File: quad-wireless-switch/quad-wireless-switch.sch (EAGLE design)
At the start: 69 parts, among them IC1 LM2937IMP-3.3, Q1 DN2625K4-G, Q2 SI2323DS-T1-E3, Q3 IRL520, Q4 IRL520, Q5 IRL520, Q6 IRL520, U1 ATMEGA328P_TQFP

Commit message: quad wireless switch wip
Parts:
- added D3, D4, D5, D6: 1N4004, diode:1N4004
- added OK1, OK2, OK3, OK4: 4N35SM, optocoupler:4N35SM
- added R24, R28, R29: 220, microbuilder:RESISTOR0805
- added R25, R26, R30, R31: 10K, microbuilder:RESISTOR0805
- added R27: 150, microbuilder:RESISTOR0805
- R10, R16: value 10k -> 10K
- R11: value 10k -> 150
- R13, R20, R21, R22: value 150 -> 220
- R14: value 10k -> 220
- R15, R23: value 150 -> 10K
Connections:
- removed net OUT2_GATE: Q4.G, R13.2
- removed net OUT3_GATE: Q5.G, R15.2
- removed net OUT4_GATE: Q6.G, R17.2
- new net N$21: OK1.COL, R25.1
- new net N$23: OK1.A, R24.1
- new net N$24: D5.A, OUT3-1.KL, Q5.D
- new net N$25: LED3.C, R21.1
- new net N$26: OK3.COL, R23.1
- new net N$27: OK3.A, R22.1
- new net N$28: OK3.EMI, R17.1, R26.2
- new net N$29: D6.A, OUT4-1.KL, Q6.D
- new net N$30: LED4.C, R28.1
- new net N$31: OK4.COL, R30.1
- new net N$32: OK4.A, R29.1
- new net N$33: OK4.EMI, R27.1, R31.2
- net 12V: now also D3.C, D4.C, D5.C, D6.C, R15.2, R23.2, R25.2, R30.2
- net GND: now also OK1.C, OK2.C, OK3.C, OK4.C, R10.1, R13.2, R16.1, R26.1, R28.2, R31.1; no longer R10.2, R11.2, R14.2, R16.2, R22.2, R23.2
- net N$18: now also OK2.A, R14.1; no longer OUT3-1.KL, Q5.D
- net N$2: now also OK1.EMI, R10.2, R12.1; no longer LED2.C, R21.1
- net N$22: now also OK2.EMI, R11.1, R16.2; no longer OUT4-1.KL, Q6.D
- net N$3: now also D4.A, OUT2-1.KL, Q4.D; no longer LED3.C, R22.1
- net N$4: now also LED2.C, R13.1; no longer LED4.C, R23.1
- net N$6: now also D3.A
- net N$8: now also OK2.COL, R15.1; no longer OUT2-1.KL, Q4.D
- net OUT1: now also R24.2; no longer R10.1, R12.1
- net OUT1_GATE: now also Q4.G, Q5.G, Q6.G, R11.2, R17.2, R27.2
- net OUT2: now also R14.2; no longer R11.1, R13.1
- net OUT3: now also R22.2; no longer R14.1, R15.1
- net OUT4: now also R29.2; no longer R16.1, R17.1
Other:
- moved on the sheet: LED1, LED2, LED3, LED4, OUT1-1, OUT1-2, OUT2-1, OUT2-2, OUT3-1, OUT3-2, OUT4-1, OUT4-2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

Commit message: wip
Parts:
- R1: value 10k -> 100k
- R10, R23, R25: value 10K -> 220
- R11, R12: value 150 -> 10k
- R14, R28, R29: value 220 -> 10K
- R17, R27: value 150 -> 10K
- R18, R19: value 10k -> 150
- R2: value 10k -> 39k
- R20, R21: value 220 -> 10k
- R3: value 100k -> 10k
- R30, R31: value 10K -> 150
- R4: value 39k -> 220
- R7: value 10k -> 220
- renumbered IN to X1, IN1 to X2, IN2 to X3, IN3 to X4, IN4 to X6, ISP to J1, NRF to JP1, SER to JP2
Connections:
- removed net N$32 (its old number): OK4.A, R29.1
- new net N$27: OK4.A, R23.1
- new net OUT2_GATE: Q3.G, R18.2
- new net OUT3_GATE: Q6.G, R31.2
- new net OUT4_GATE: Q5.G, R30.2
- net 12V: now also R1.2, R17.2, R27.2, R29.2; no longer R23.2, R25.2, R3.2, R30.2
- net 3.3V: now also R11.1, R12.1, R20.1, R21.1, R3.2; no longer R1.1, R18.1, R19.1, R2.1, R7.2
- net CSN: now also R5.1; no longer R7.1
- net GND: now also R10.2, R14.1, R2.2, R24.2, R25.2, R28.1; no longer R10.1, R20.2, R21.2, R28.2, R31.1, R4.2
- net IN1: now also R11.2; no longer R1.2
- net IN2: now also R12.2; no longer R2.2
- net IN3: now also R20.2; no longer R18.2
- net IN4: now also R21.2; no longer R19.2
- net MISO: now also R6.1; no longer R8.1
- net MOSI: now also R4.2; no longer R6.2
- net N$1: now also R13.1; no longer R20.1
- net N$11: now also R1.1; no longer R3.1
- net N$14: now also R2.1; no longer R4.1
- net N$18: now also OK1.A, R8.1; no longer OK2.A, R14.1
- net N$2: now also OK2.EMI, R16.2, R19.1; no longer OK1.EMI, R10.2, R12.1
- net N$21: now also OK2.COL, R17.1; no longer OK1.COL, R25.1
- net N$22: now also OK1.EMI, R14.2, R18.1; no longer OK2.EMI, R11.1, R16.2
- net N$23: now also OK2.A, R9.1; no longer OK1.A, R24.1
- net N$24: now also D6.A, Q6.D; no longer D5.A, Q5.D
- net N$25: now also R25.1; no longer R21.1
- net N$26: now also OK4.COL, R29.1; no longer OK3.COL, R23.1
- net N$28: now also OK4.EMI, R28.2, R31.1; no longer OK3.EMI, R17.1, R26.2
- net N$29: now also D5.A, Q5.D; no longer D6.A, Q6.D
- net N$3: now also D3.A, Q3.D; no longer D4.A, Q4.D
- net N$30: now also R24.1; no longer R28.1
- net N$31: now also OK3.COL, R27.1; no longer OK4.COL, R30.1
- net N$33: now also OK3.EMI, R26.2, R30.1; no longer OK4.EMI, R27.1, R31.2
- net N$4: now also R10.1; no longer R13.1
- net N$6: now also D4.A, Q4.D; no longer D3.A, Q3.D
- net N$66: now also R7.2; no longer R9.2
- net N$7: now also R4.1; no longer R6.1
- net N$8: now also OK1.COL; no longer OK2.COL
- net N$9: now also R6.2; no longer R8.2
- net OUT1: now also R9.2; no longer R24.2
- net OUT1_GATE: now also R19.2; no longer Q3.G, Q5.G, Q6.G, R11.2, R12.2, R17.2, R27.2
- net OUT2: now also R8.2; no longer R14.2
- net OUT3: now also R23.2; no longer R22.2
- net OUT4: now also R22.2; no longer R29.2
- net RESET: now also R3.1; no longer R5.1
- net SCK: now also R7.1; no longer R9.1
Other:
- moved on the sheet: D3, D4, D5, D6, OK1, OK2, OK3, OK4, Q3, Q4, Q5, Q6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

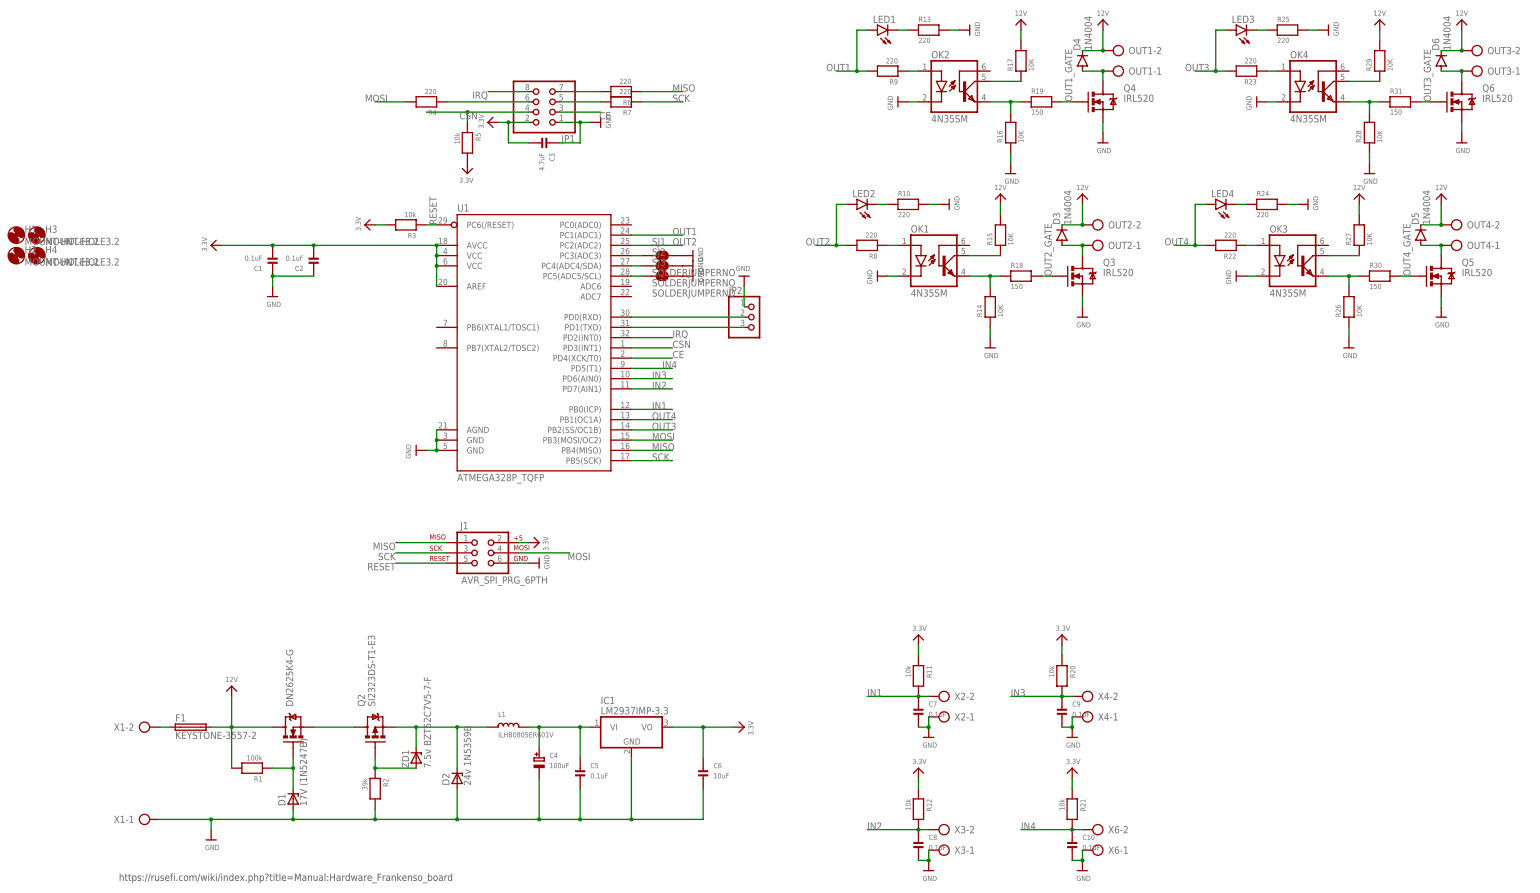
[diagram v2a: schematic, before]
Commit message: quad wireless switch with nrf24
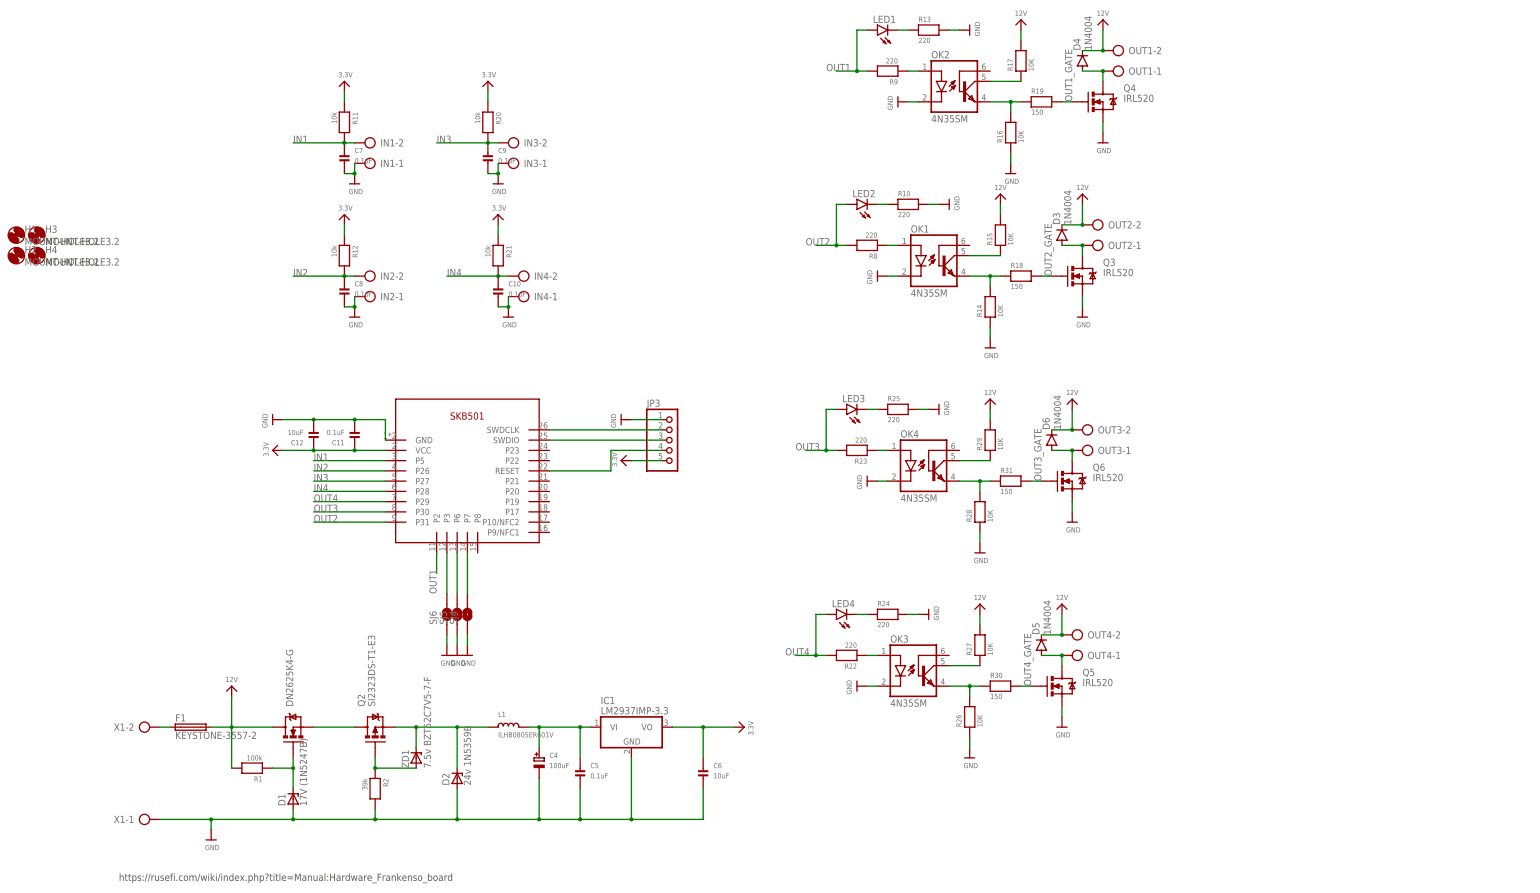
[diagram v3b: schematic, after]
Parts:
- removed C1, C2: 0.1uF, microbuilder:CAP_CERAMIC0805
- removed C3: 4.7uF, microbuilder:CAP_CERAMIC0805
- removed J1: AVR_SPI_PRG_6PTH, SparkFun-Connectors:AVR_SPI_PRG_6PTH
- removed JP1: (no value), pinhead:PINHD-2X4
- removed JP2: (no value), pinhead:PINHD-1X3
- removed R3, R5: 10k, microbuilder:RESISTOR0805
- removed R4, R6, R7: 220, microbuilder:RESISTOR0805
- removed SJ1, SJ2, SJ3: SOLDERJUMPERNO, SparkFun-Retired:SOLDERJUMPERNO
- removed U1: ATMEGA328P_TQFP, SparkFun-DigitalIC:ATMEGA328P_TQFP
- removed X2, X3, X4, X6: (no value), con-ptr500:AK500/2-H
- added C11: 0.1uF, microbuilder:CAP_CERAMIC0805
- added C12: 10uF, microbuilder:CAP_CERAMIC0805
- added IN1, IN2, IN3, IN4: (no value), con-ptr500:AK500/2-H
- added JP3: (no value), pinhead:PINHD-1X5
- added SJ4, SJ5, SJ6: SOLDERJUMPERNO, SparkFun-Retired:SOLDERJUMPERNO
- added U2: SDB501, shlomo:SDB501
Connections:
- removed net CE: JP1.3, U1.PD4(XCK/T0)
- removed net CSN: JP1.4, R5.1, U1.PD3(INT1)
- removed net IRQ: JP1.8, U1.PD2(INT0)
- removed net MISO: J1.1, R6.1, U1.PB4(MISO)
- removed net MOSI: J1.4, R4.2, U1.PB3(MOSI/OC2)
- removed net N$12: SJ2.1, U1.PC4(ADC4/SDA)
- removed net N$16: SJ3.1, U1.PC5(ADC5/SCL)
- removed net N$19: JP2.3, U1.PD1(TXD)
- removed net N$20: JP2.2, U1.PD0(RXD)
- removed net N$66: JP1.5, R7.2
- removed net RESET: J1.5, R3.1, U1.PC6(/RESET)
- removed net SCK: J1.3, R7.1, U1.PB5(SCK)
- new net N$36: JP3.2, U2.SWDCLK
- new net N$37: JP3.3, U2.SWDIO
- new net N$38: JP3.4, U2.RESET
- net 3.3V: now also C11.P$1, C12.P$1, JP3.5, U2.VCC; no longer C1.P$2, C2.P$2, C3.P$2, J1.2, JP1.2, R3.2, R5.2, U1.AREF, U1.AVCC, U1.VCC@4, U1.VCC@6
- net GND: now also C11.P$2, C12.P$2, IN1-1.KL, IN2-1.KL, IN3-1.KL, IN4-1.KL, JP3.1, SJ4.1, SJ5.1, SJ6.1, U2.GND; no longer C1.P$1, C2.P$1, C3.P$1, J1.6, JP1.1, JP2.1, SJ1.2, SJ2.2, SJ3.2, U1.AGND, U1.GND@3, U1.GND@5, X2-1.KL, X3-1.KL, X4-1.KL, X6-1.KL
- net IN1: now also IN1-2.KL, U2.P5; no longer U1.PB0(ICP), X2-2.KL
- net IN2: now also IN2-2.KL, U2.P26; no longer U1.PD7(AIN1), X3-2.KL
- net IN3: now also IN3-2.KL, U2.P27; no longer U1.PD6(AIN0), X4-2.KL
- net IN4: now also IN4-2.KL, U2.P28; no longer U1.PD5(T1), X6-2.KL
- net N$10: now also SJ6.2, U2.P3; no longer SJ1.1, U1.PC3(ADC3)
- net N$7: now also SJ4.2, U2.P7; no longer JP1.6, R4.1
- net N$9: now also SJ5.2, U2.P6; no longer JP1.7, R6.2
- net OUT1: now also U2.P2; no longer U1.PC1(ADC1)
- net OUT2: now also U2.P31; no longer U1.PC2(ADC2)
- net OUT3: now also U2.P30; no longer U1.PB2(SS/OC1B)
- net OUT4: now also U2.P29; no longer U1.PB1(OC1A)
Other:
- moved on the sheet: C10, C7, C8, C9, D5, D6, LED3, LED4, OK3, OK4, OUT3-1, OUT3-2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

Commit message: wip
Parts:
- added JP1: (no value), pinhead:PINHD-1X2
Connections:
- net 3.3V: now also JP1.2
- net GND: now also JP1.1
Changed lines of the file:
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@@
 <part name="GND33" library="microbuilder" deviceset="GND" device=""/>
 <part name="GND34" library="microbuilder" deviceset="GND" device=""/>
+<part name="JP1" library="pinhead" library_urn="urn:adsk.eagle:library:325" deviceset="PINHD-1X2" device="" package3d_urn="urn:adsk.eagle:package:22435/2"/>
+<part name="GND2" library="microbuilder" deviceset="GND" device=""/>
+<part name="3.3V1" library="microbuilder" deviceset="3.3V" device=""/>
 </parts>
 <sheets>
@@
 <instance part="GND34" gate="G$1" x="149.86" y="17.78" smashed="yes">
 <attribute name="VALUE" x="148.336" y="15.24" size="1.27" layer="96"/>
+</instance>
+<instance part="JP1" gate="G$1" x="83.82" y="88.9" smashed="yes" rot="R180">
+<attribute name="NAME" x="90.17" y="83.185" size="1.778" layer="95" rot="R180"/>
+<attribute name="VALUE" x="90.17" y="93.98" size="1.778" layer="96" rot="R180"/>
+</instance>
+<instance part="GND2" gate="G$1" x="96.52" y="86.36" smashed="yes" rot="R90">
+<attribute name="VALUE" x="99.06" y="84.836" size="1.27" layer="96" rot="R90"/>
+</instance>
+<instance part="3.3V1" gate="G$1" x="96.52" y="88.9" smashed="yes" rot="R270">
+<attribute name="VALUE" x="97.536" y="90.424" size="1.27" layer="96" rot="R270"/>
 </instance>
 </instances>
@@
 <wire x1="149.86" y1="22.86" x2="149.86" y2="20.32" width="0.1524" layer="91"/>
 </segment>
+<segment>
+<pinref part="JP1" gate="G$1" pin="1"/>
+<pinref part="GND2" gate="G$1" pin="GND"/>
+<wire x1="93.98" y1="86.36" x2="86.36" y2="86.36" width="0.1524" layer="91"/>
+</segment>
 </net>
 <net name="3.3V" class="0">
@@
 <wire x1="190.5" y1="66.04" x2="198.12" y2="66.04" width="0.1524" layer="91"/>
 </segment>
+<segment>
+<pinref part="JP1" gate="G$1" pin="2"/>
+<pinref part="3.3V1" gate="G$1" pin="3.3V"/>
+<wire x1="93.98" y1="88.9" x2="86.36" y2="88.9" width="0.1524" layer="91"/>
+</segment>
 </net>
